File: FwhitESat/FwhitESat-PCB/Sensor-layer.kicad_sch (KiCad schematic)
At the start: 4 parts, among them U3 DS1307_, U7 MPU-6050

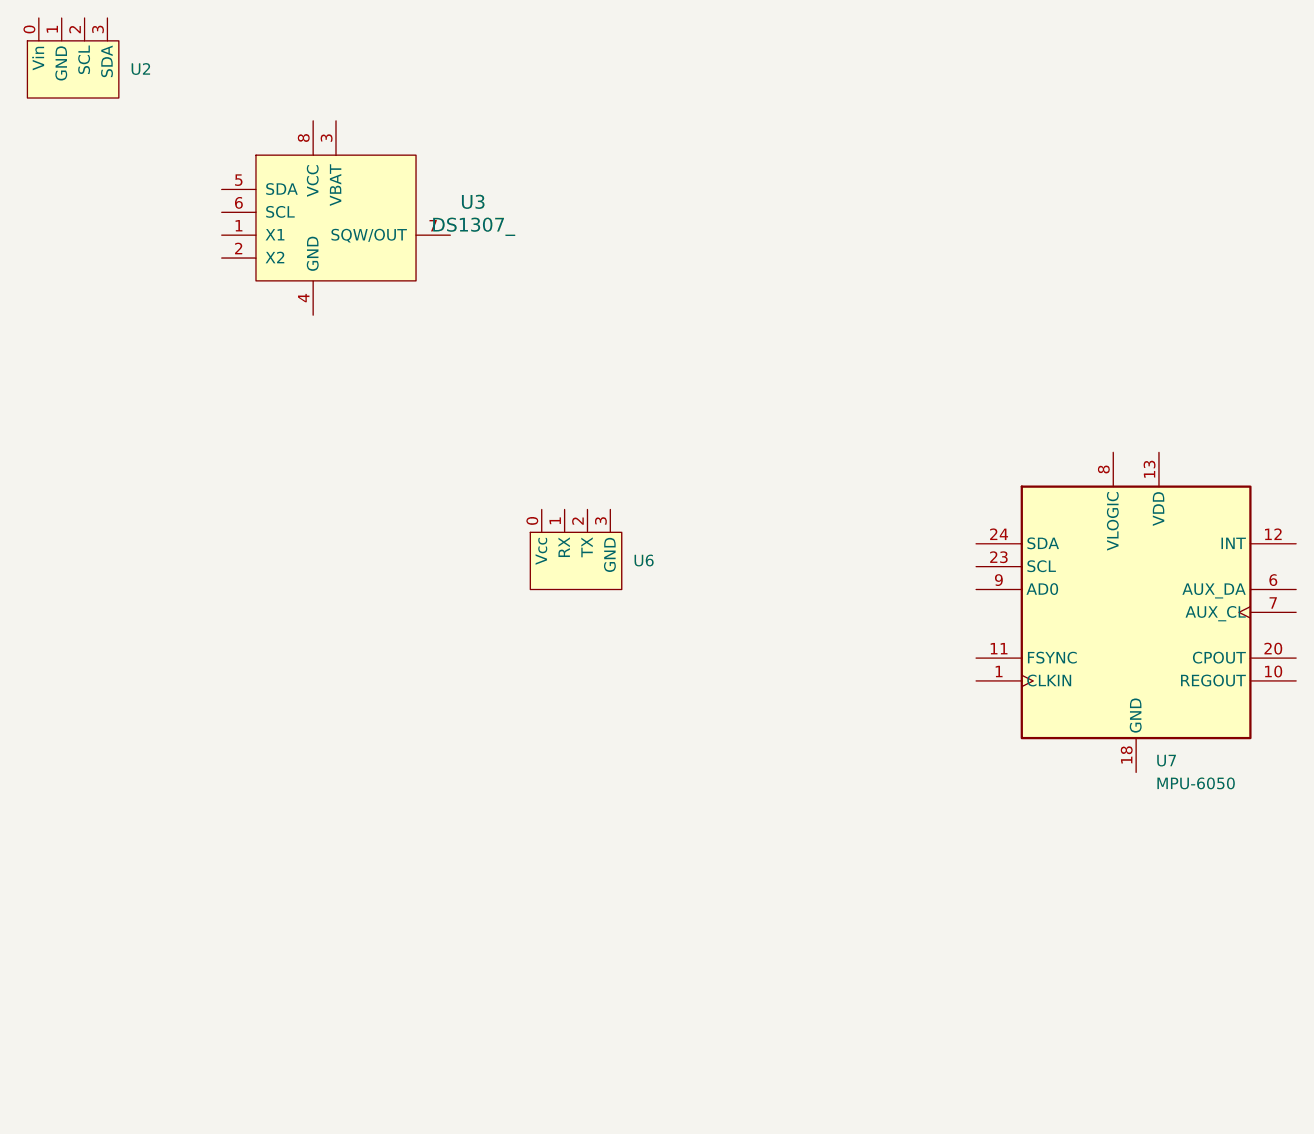
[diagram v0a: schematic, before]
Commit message: fix FwhitESat/FwhitESat-PCB
add I2C line.
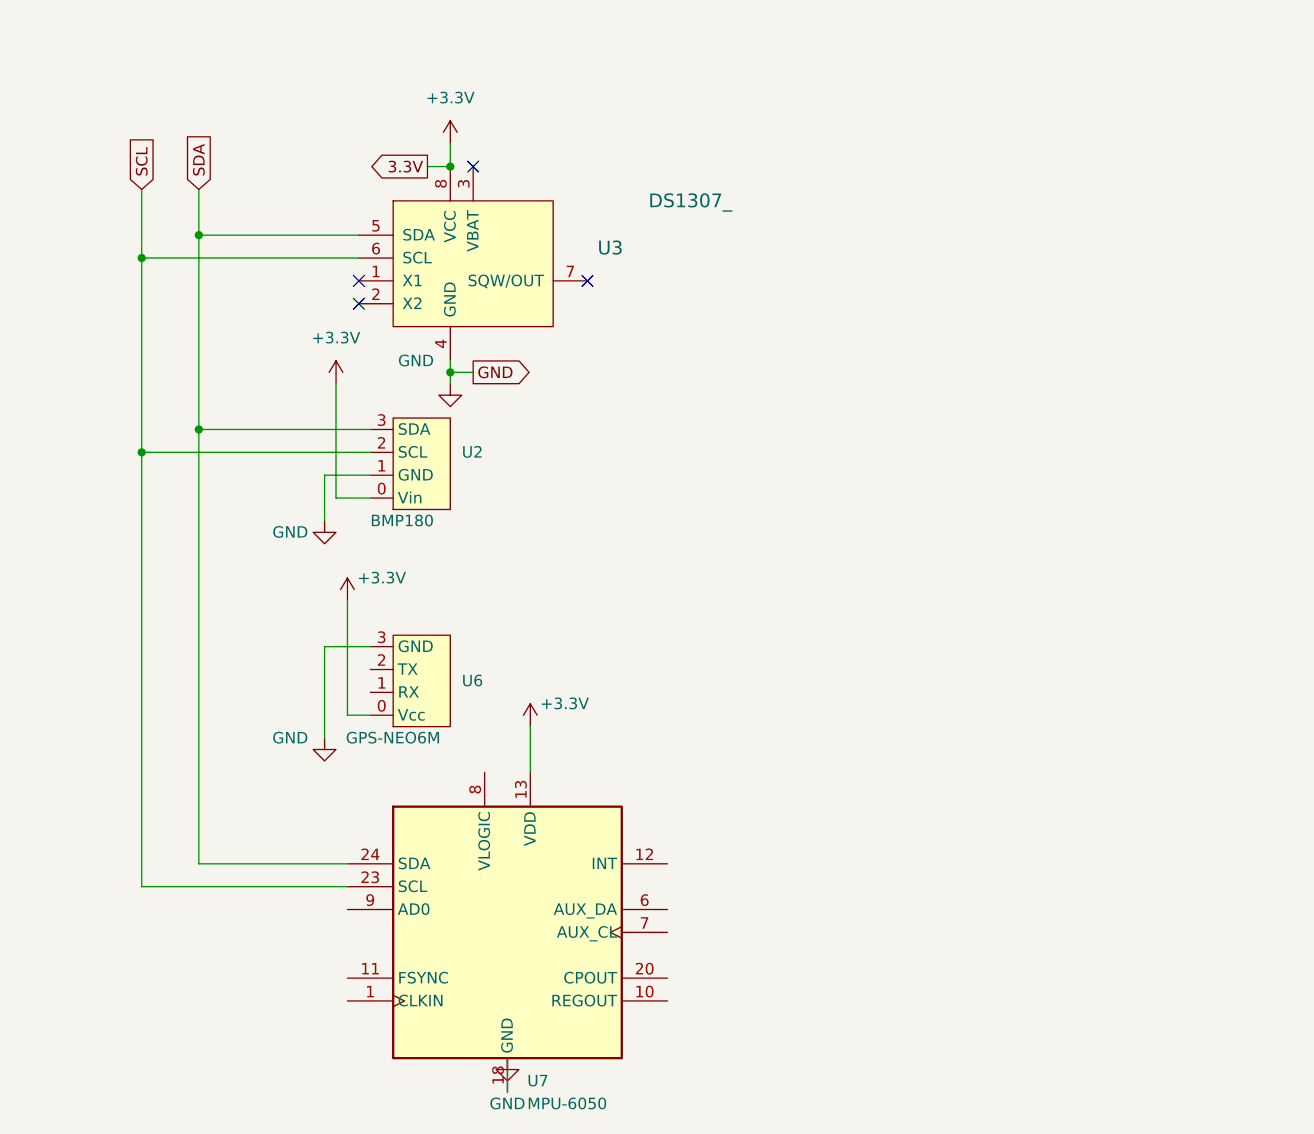
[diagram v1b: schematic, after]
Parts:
- U2: value ~ -> BMP180
- U6: value ~ -> GPS-NEO6M
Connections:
- net GND: now reaches U3.4 (GND)
- net GND: now also U2.1 (GND), U6.3 (GND), U7.18 (GND)
- net SDA: now reaches U3.5 (SDA)
- net SDA: now also U2.3 (SDA), U7.24 (SDA)
- net SCL: now reaches U3.6 (SCL)
- net SCL: now also U2.2 (SCL), U7.23 (SCL)
- net +3.3V: now reaches U3.8 (VCC)
- net +3.3V: now also U2.0 (Vin), U6.0 (Vcc), U7.13 (VDD)
- no-connect marks 0 -> 4
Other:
- moved on the sheet: U2, U3, U6, U7

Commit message: おなかすいた
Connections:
- net +3.3V: no longer U3.8 (VCC), U6.0 (Vcc)
- net GND: no longer U6.3 (GND)
- new net +5V: U3.8 (VCC)
- no-connect marks 4 -> 12
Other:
- note added: "I2C part"
- note added: "Sensor layer"
- note added: "UART part"
- moved on the sheet: U2, U6, U7

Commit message: くっぱ
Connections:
- net +3.3V: now also U6.0 (Vcc)
- net GND: now also U6.3 (GND)
- net GPSRX: now reaches U6.1 (RX)
- net GPSTX: now reaches U6.2 (TX)
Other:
- note added: "Note: GPSはハードウェアシリアル でないとうまく動かない"
- note added: "Note: I2Cのプルアップ抵抗が不安かも"
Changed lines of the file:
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@@
   (junction (at 144.78 73.66) (diameter 0) (color 0 0 0 0)
   )
+  (junction (at 217.17 76.2) (diameter 0) (color 0 0 0 0)
+  )
   (junction (at 80.01 82.55) (diameter 0) (color 0 0 0 0)
   )
@@
   )
   (junction (at 95.25 73.66) (diameter 0) (color 0 0 0 0)
+  )
+  (junction (at 214.63 73.66) (diameter 0) (color 0 0 0 0)
   )
   (no_connect (at 144.78 102.87))
@@
     (stroke (width 0) (type default))
   )
+  (wire (pts (xy 219.71 80.01) (xy 219.71 82.55))
+    (stroke (width 0) (type default))
+  )
   (wire (pts (xy 113.03 91.44) (xy 113.03 82.55))
     (stroke (width 0) (type default))
@@
     (stroke (width 0) (type default))
   )
+  (wire (pts (xy 190.5 76.2) (xy 217.17 76.2))
+    (stroke (width 0) (type default))
+  )
+  (wire (pts (xy 226.06 80.01) (xy 226.06 100.33))
+    (stroke (width 0) (type default))
+  )
   (wire (pts (xy 101.6 87.63) (xy 110.49 87.63))
     (stroke (width 0) (type default))
@@
     (stroke (width 0) (type default))
   )
+  (wire (pts (xy 219.71 80.01) (xy 226.06 80.01))
+    (stroke (width 0) (type default))
+  )
   (wire (pts (xy 115.57 77.47) (xy 115.57 91.44))
     (stroke (width 0) (type default))
@@
     (stroke (width 0) (type default))
   )
+  (wire (pts (xy 217.17 76.2) (xy 223.52 76.2))
+    (stroke (width 0) (type default))
+  )
   (wire (pts (xy 123.19 100.33) (xy 123.19 127))
     (stroke (width 0) (type default))
@@
     (stroke (width 0) (type default))
   )
+  (wire (pts (xy 214.63 73.66) (xy 223.52 73.66))
+    (stroke (width 0) (type default))
+  )
   (wire (pts (xy 134.62 82.55) (xy 134.62 90.17))
     (stroke (width 0) (type default))
   )
+  (wire (pts (xy 214.63 73.66) (xy 214.63 82.55))
+    (stroke (width 0) (type default))
+  )
+  (wire (pts (xy 217.17 76.2) (xy 217.17 82.55))
+    (stroke (width 0) (type default))
+  )
   (wire (pts (xy 144.78 73.66) (xy 144.78 100.33))
     (stroke (width 0) (type default))
   )
+  (wire (pts (xy 212.09 69.85) (xy 212.09 82.55))
+    (stroke (width 0) (type default))
+  )
   (wire (pts (xy 107.95 73.66) (xy 107.95 91.44))
     (stroke (width 0) (type default))
@@
     (stroke (width 0) (type default))
   )
+  (wire (pts (xy 190.5 73.66) (xy 214.63 73.66))
+    (stroke (width 0) (type default))
+  )
   (wire (pts (xy 49.53 77.47) (xy 82.55 77.47))
     (stroke (width 0) (type default))
@@
     (fill (type none))
   )
-  (rectangle (start 26.67 46.99) (end 161.29 147.32)
+  (rectangle (start 26.67 46.99) (end 161.29 172.72)
     (stroke (width 0) (type default))
     (fill (type none))
   )
-  (text "Sensor layer" (at 26.67 33.02 0)
+  (text "Note:\nI2Cのプルアップ抵抗が不安かも" (at 102.87 165.1 0)
+    (effects (font (size 3 3)) (justify left bottom))
+  )
+  (text "Sensor layer" (at 15.24 21.59 0)
     (effects (font (size 5 5)) (justify left bottom))
+  )
+  (text "Note:\nGPSはハードウェアシリアル\nでないとうまく動かない" (at 236.22 139.7 0)
+    (effects (font (size 3 3)) (justify left bottom))
   )
   (text "I2C part" (at 43.18 59.69 0)
@@
   (text "UART part" (at 172.72 59.69 0)
     (effects (font (size 5 5)) (justify left bottom))
+  )
+  (global_label "GPSTX" (shape input) (at 223.52 76.2 0) (fields_autoplaced)
+    (effects (font (size 1.27 1.27)) (justify left))
+    (property "Intersheetrefs" "${INTERSHEET_REFS}" (at 232.4318 76.2 0)
+      (effects (font (size 1.27 1.27)) (justify left) hide)
+    )
   )
   (global_label "3.3V" (shape input) (at 91.44 73.66 180) (fields_autoplaced)
@@
     (property "Intersheetrefs" "${INTERSHEET_REFS}" (at 43.0372 82.55 0)
       (effects (font (size 1.27 1.27)) (justify right) hide)
+    )
+  )
+  (global_label "RasRX" (shape input) (at 190.5 76.2 180) (fields_autoplaced)
+    (effects (font (size 1.27 1.27)) (justify right))
+    (property "Intersheetrefs" "${INTERSHEET_REFS}" (at 181.5882 76.2 0)
+      (effects (font (size 1.27 1.27)) (justify right) hide)
+    )
+  )
+  (global_label "RasTX" (shape input) (at 190.5 73.66 180) (fields_autoplaced)
+    (effects (font (size 1.27 1.27)) (justify right))
+    (property "Intersheetrefs" "${INTERSHEET_REFS}" (at 181.8906 73.66 0)
+      (effects (font (size 1.27 1.27)) (justify right) hide)
+    )
+  )
+  (global_label "GPSRX" (shape input) (at 223.52 73.66 0) (fields_autoplaced)
+    (effects (font (size 1.27 1.27)) (justify left))
+    (property "Intersheetrefs" "${INTERSHEET_REFS}" (at 232.7342 73.66 0)
+      (effects (font (size 1.27 1.27)) (justify left) hide)
+    )
+  )
+  (symbol (lib_id "power:GND") (at 226.06 100.33 0) (unit 1)
+    (in_bom yes) (on_board yes) (dnp no) (fields_autoplaced)
+    (property "Reference" "#PWR08" (at 226.06 106.68 0)
+      (effects (font (size 1.27 1.27)) hide)
+    )
+    (property "Value" "GND" (at 226.06 105.41 0)
+      (effects (font (size 1.27 1.27)))
+    )
+    (property "Footprint" "" (at 226.06 100.33 0)
+      (effects (font (size 1.27 1.27)) hide)
+    )
+    (property "Datasheet" "" (at 226.06 100.33 0)
+      (effects (font (size 1.27 1.27)) hide)
+    )
+    (pin "1")
+    (instances
+      (project "FwhitESat-PCB"
+        (path "/78ea2883-2db0-4d81-80e1-b63c1c2056ac"
+          (reference "#PWR08") (unit 1)
+        )
+        (path "/78ea2883-2db0-4d81-80e1-b63c1c2056ac/56957d94-f740-47f0-918d-81f554d7e663"
+          (reference "#PWR015") (unit 1)
+        )
+        (path "/78ea2883-2db0-4d81-80e1-b63c1c2056ac/20bd63c0-c7d9-415e-b9da-e5b49e44652d"
+          (reference "#PWR017") (unit 1)
+        )
+      )
     )
   )
@@
       (effects (font (size 1.27 1.27)) (justify right))
     )
-    (property "Value" "GPS-NEO6M" (at 209.55 85.09 90)
+    (property "Value" "GPS-NEO6M" (at 208.28 93.98 0)
       (effects (font (size 1.27 1.27)))
     )
@@
         )
       )
+    )
+  )
+  (symbol (lib_id "power:+3.3V") (at 212.09 69.85 0) (unit 1)
+    (in_bom yes) (on_board yes) (dnp no) (fields_autoplaced)
+    (property "Reference" "#PWR07" (at 212.09 73.66 0)
+      (effects (font (size 1.27 1.27)) hide)
+    )
+    (property "Value" "+3.3V" (at 212.09 64.77 0)
+      (effects (font (size 1.27 1.27)))
+    )
+    (property "Footprint" "" (at 212.09 69.85 0)
+      (effects (font (size 1.27 1.27)) hide)
+    )
+    (property "Datasheet" "" (at 212.09 69.85 0)
+      (effects (font (size 1.27 1.27)) hide)
+    )
+    (pin "1")
+    (instances
+      (project "FwhitESat-PCB"
+        (path "/78ea2883-2db0-4d81-80e1-b63c1c2056ac"
+          (reference "#PWR07") (unit 1)
+        )
+        (path "/78ea2883-2db0-4d81-80e1-b63c1c2056ac/56957d94-f740-47f0-918d-81f554d7e663"
+          (reference "#PWR016") (unit 1)
+        )
+        (path "/78ea2883-2db0-4d81-80e1-b63c1c2056ac/20bd63c0-c7d9-415e-b9da-e5b49e44652d"
+          (reference "#PWR08") (unit 1)
+        )
+      )
